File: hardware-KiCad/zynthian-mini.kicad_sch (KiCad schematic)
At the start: 76 parts, among them J1 NEUTRIK, J2 RCA RS-234, SW1 SW_Push, SW10 SW_Push, SW11 SW_Push, SW12 SW_Push, SW13 SW_Push, SW14 SW_Push, SW15 SW_Push, SW16 SW_Push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

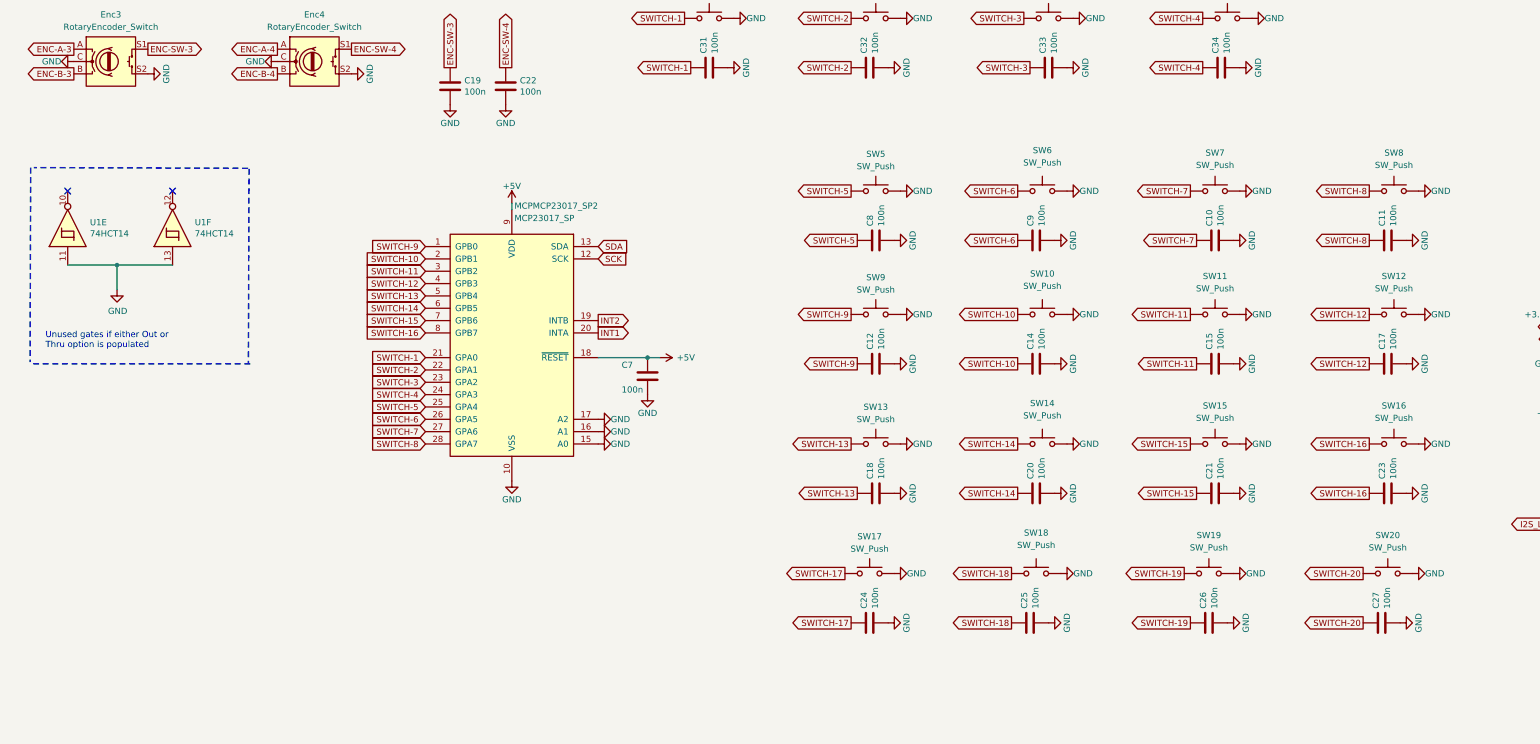
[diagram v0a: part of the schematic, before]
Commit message: added encoder de bouncing caps
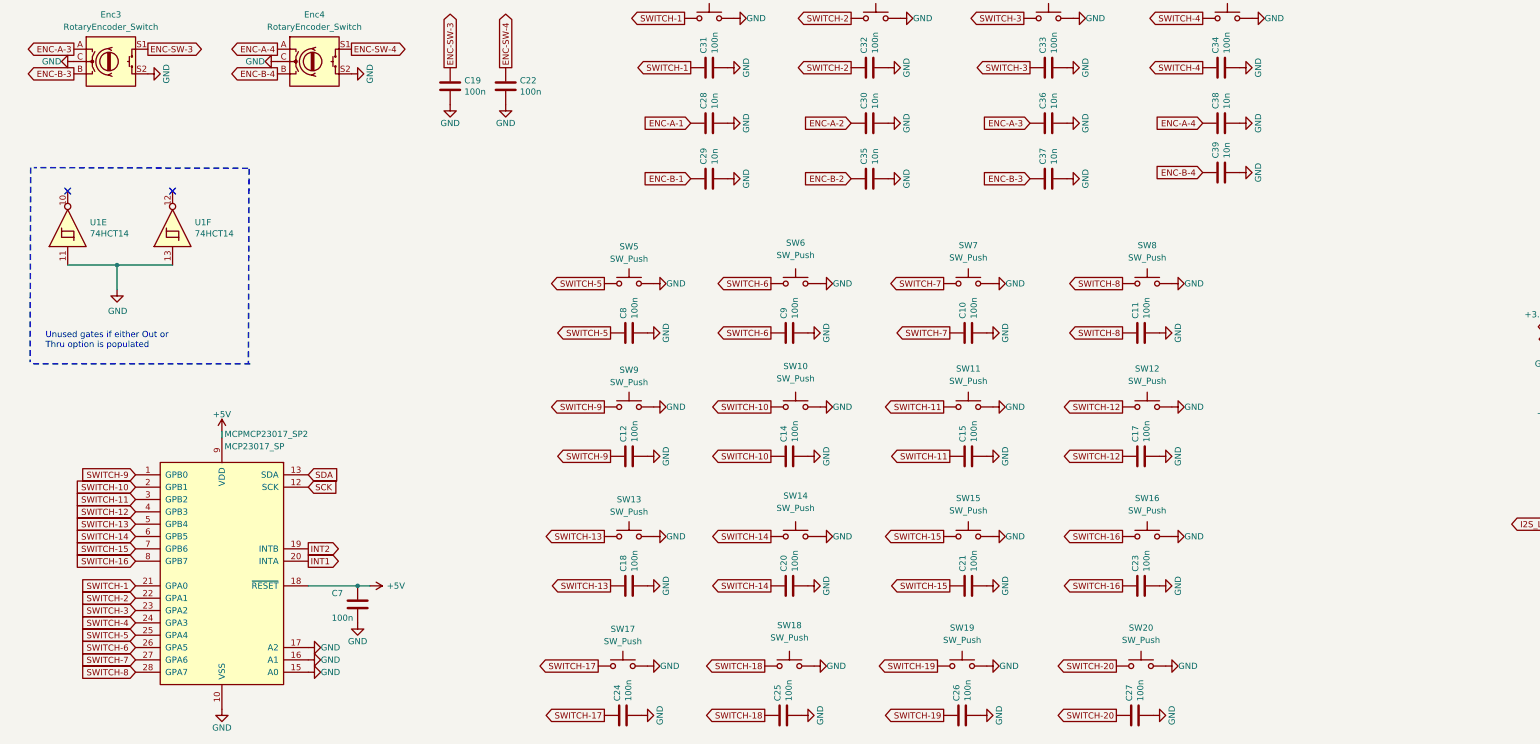
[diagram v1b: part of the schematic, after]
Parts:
- added C28, C29, C30, C35, C36, C37, C38, C39: 10n, Capacitor_THT:C_Rect_L4.0mm_W2.5mm_P2.50mm, symbol Device:C
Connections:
- net ENC-A-1: now also C28.1
- net ENC-A-2: now also C30.1
- net ENC-A-3: now also C36.1
- net ENC-A-4: now also C38.1
- net ENC-B-1: now also C29.1
- net ENC-B-2: now also C35.1
- net ENC-B-3: now also C37.1
- net ENC-B-4: now also C39.1
- net GND: now also C28.2, C29.2, C30.2, C35.2, C36.2, C37.2, C38.2, C39.2
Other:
- moved on the sheet: C10, C11, C12, C14, C15, C17, C18, C20, C21, C23, C24, C25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
